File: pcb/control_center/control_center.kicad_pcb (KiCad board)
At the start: 2 copper layers, 99.1 x 99.1 mm, 52 parts, among them SW1 SW_Push, SW2 SW_Push, U1 STM32F031C6Tx, U2 AMS1117-3.3, U3 AMS1117-5.0, Y1 8M, Y2 32768HZ

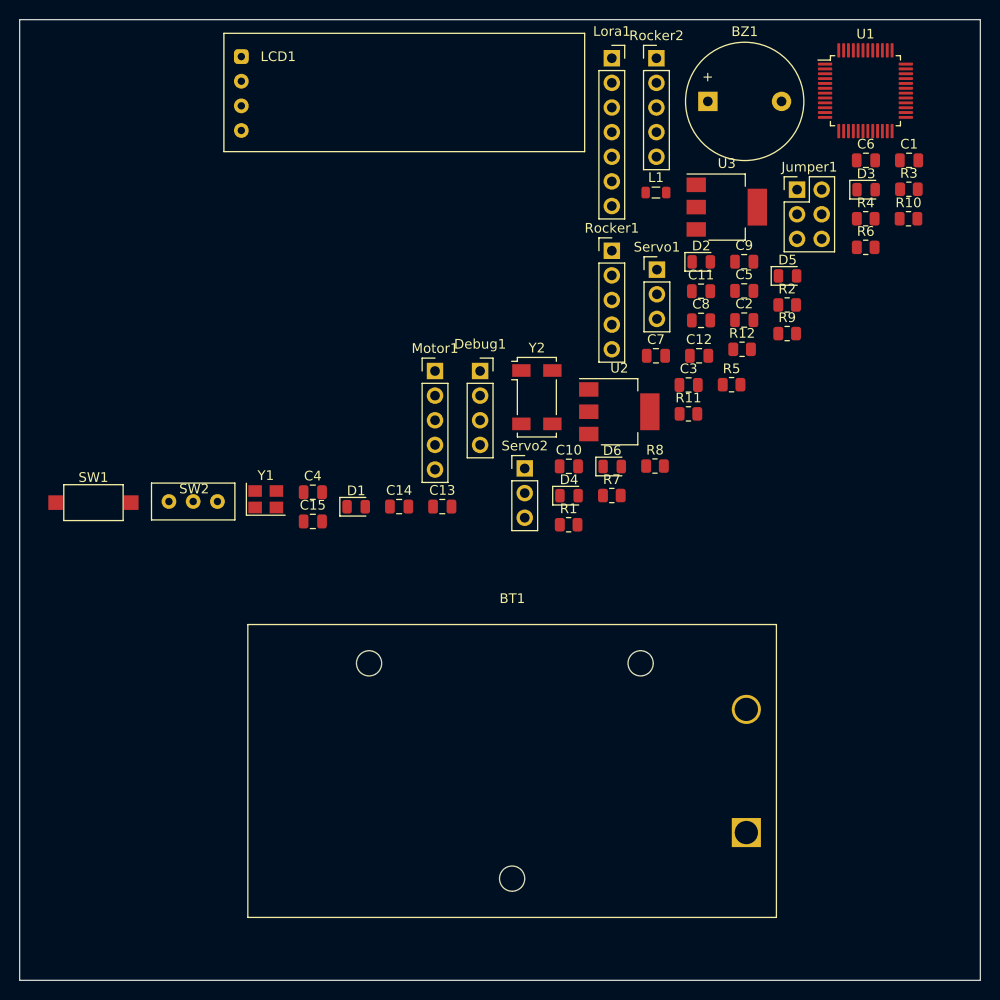
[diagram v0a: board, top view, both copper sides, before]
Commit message: Layout control_center board.
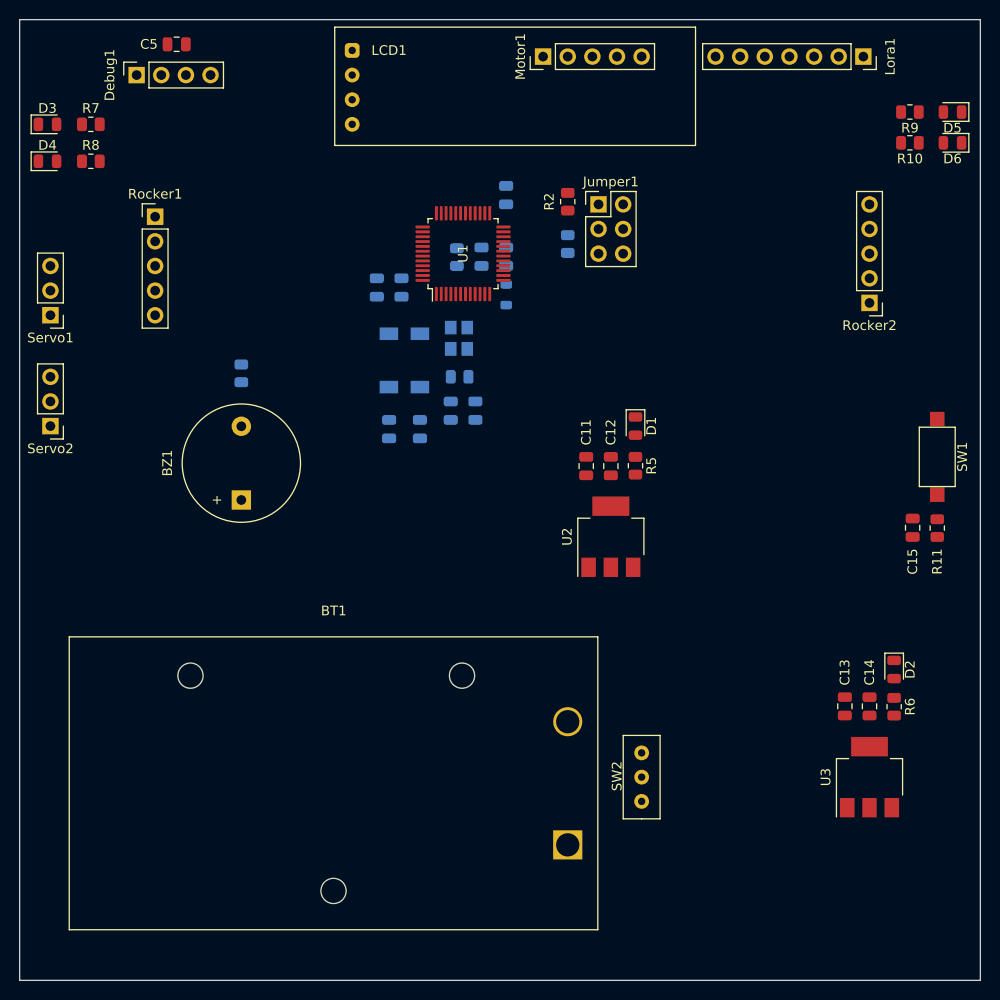
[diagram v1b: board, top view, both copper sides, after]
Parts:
- C1, C10, C2, C3, C4, C6, C7, C8, C9, L1, R1, R12, R3, R4, Y1, Y2: moved to B.Cu
- moved SW1 87.1 mm to (132.7, 70.5), turned to 270 degrees
- moved D3 84.7 mm to (41.0, 36.2)
- moved R8 66.1 mm to (45.4, 40.0)
- moved R7 66.0 mm to (45.4, 36.2)
- moved D4 63.9 mm to (41.0, 40.0)
- moved C5 63.8 mm to (54.3, 27.9), turned to 180 degrees
- moved BZ1 63.3 mm to (61.0, 74.9), turned to 90 degrees
- moved Servo1 62.7 mm to (41.3, 55.9), turned to 180 degrees
- moved C15 61.8 mm to (130.2, 77.8), turned to 270 degrees
- moved U3 60.6 mm to (125.7, 103.5), turned to 90 degrees
- moved SW2 54.3 mm to (102.2, 103.5), turned to 90 degrees
- moved C1 53.8 mm to (82.5, 65.7), turned to 90 degrees
- moved C14 52.7 mm to (125.7, 96.2), turned to 90 degrees
- moved R12 51.7 mm to (61.0, 61.9), turned to 270 degrees
- moved R3 50.2 mm to (83.5, 62.2), turned to 180 degrees
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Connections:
- Debug1 pad 2: /SYS_JTCK-SWCL -> /SYS_SWCL
- Debug1 pad 3: /SYS_JTMS-SWDIO -> /SYS_SWDIO

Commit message: Update layout for control center board.
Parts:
- Y1: footprint Crystal:Crystal_SMD_Abracon_ABM8G-4Pin_3.2x2.5mm -> Crystal:Crystal_SMD_3225-4Pin_3.2x2.5mm
- moved R11 46.1 mm to (92.1, 56.2), turned to 90 degrees
- moved C15 41.6 mm to (94.6, 56.2), turned to 90 degrees
- moved SW1 41.2 mm to (92.1, 63.5), turned to 90 degrees
- moved C13 37.6 mm to (115.6, 59.4)
- moved R6 37.6 mm to (120.7, 59.4)
- moved C14 37.6 mm to (118.1, 59.4)
- moved D2 37.6 mm to (120.7, 55.6)
- moved U3 37.6 mm to (118.1, 66.7)
- moved Servo1 13.3 mm to (41.3, 69.2)
- moved Servo2 13.3 mm to (41.3, 80.6)
- moved C11 12.7 mm to (100.3, 59.4)
- moved C12 12.7 mm to (102.9, 59.4)
- moved D1 12.7 mm to (105.4, 55.2)
- moved U2 12.7 mm to (102.9, 66.7)
- moved R5 12.7 mm to (105.4, 59.3)
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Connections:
- LCD1 pad 2: /I2C1_SDA -> /V3.3
- LCD1 pad 4: /V3.3 -> /I2C1_SDA
- Y1 pad 3: Net-(Y1-Pad3) -> /RCC_OSC_OUT
- Y1 pad 4: /RCC_OSC_OUT -> Net-(Y1-Pad4)
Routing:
- net /V5.0: track 0.00 -> 81.8 mm

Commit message: Update control center board.
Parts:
- added Pad1: MountingHole_3mm_Pad_Via, MountingHole:MountingHole_3mm_Pad_Via, F.Cu at (41.9, 29.2)
- added Pad2: MountingHole_3mm_Pad_Via, MountingHole:MountingHole_3mm_Pad_Via, F.Cu at (133.3, 29.2)
- added Pad3: MountingHole_3mm_Pad_Via, MountingHole:MountingHole_3mm_Pad_Via, F.Cu at (41.9, 120.7)
- added Pad4: MountingHole_3mm_Pad_Via, MountingHole:MountingHole_3mm_Pad_Via, F.Cu at (133.3, 120.7)
- L1, R4: moved to F.Cu
- moved L1 37.3 mm to (122.9, 67.5)
- moved R4 33.9 mm to (115.4, 60.4), turned to 90 degrees
- moved Servo2 30.5 mm to (52.1, 52.1), turned to 90 degrees
- moved D1 30.3 mm to (118.2, 82.7), turned to 90 degrees
- moved Servo1 25.3 mm to (52.1, 46.4), turned to 90 degrees
- moved D3 24.8 mm to (65.1, 41.9)
- moved D4 24.8 mm to (65.1, 45.7)
- moved R7 24.8 mm to (69.6, 41.9)
- moved R8 24.8 mm to (69.6, 45.7)
- moved R5 23.1 mm to (118.2, 78.6), turned to 90 degrees
- moved R10 19.7 mm to (111.5, 45.1)
- moved R9 19.7 mm to (111.5, 41.9)
- moved D5 19.7 mm to (115.9, 41.9)
- moved D6 19.7 mm to (115.9, 45.1)
- moved C11 15.9 mm to (115.4, 64.2)
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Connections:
- Rocker1 pad 1: GND -> GNDA
- Rocker1 pad 2: /V5.0 -> +3.3VA
- Rocker2 pad 1: GND -> GNDA
- Rocker2 pad 2: /V5.0 -> +3.3VA
- Y1 pad 2: Net-(Y1-Pad2) -> GND
- Y1 pad 4: Net-(Y1-Pad4) -> GND
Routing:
- net /V5.0: track 81.8 -> 0.00 mm
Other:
- net class VCC added: clearance 0.2, trace_width 0.5, via_dia 0.8, via_drill 0.4
